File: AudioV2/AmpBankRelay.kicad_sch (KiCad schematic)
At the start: 20 parts, among them K301 AZ850P2-5, K302 AZ850P2-5, K303 AZ850P2-5, K304 AZ850P2-5, U321 TBD62083APG

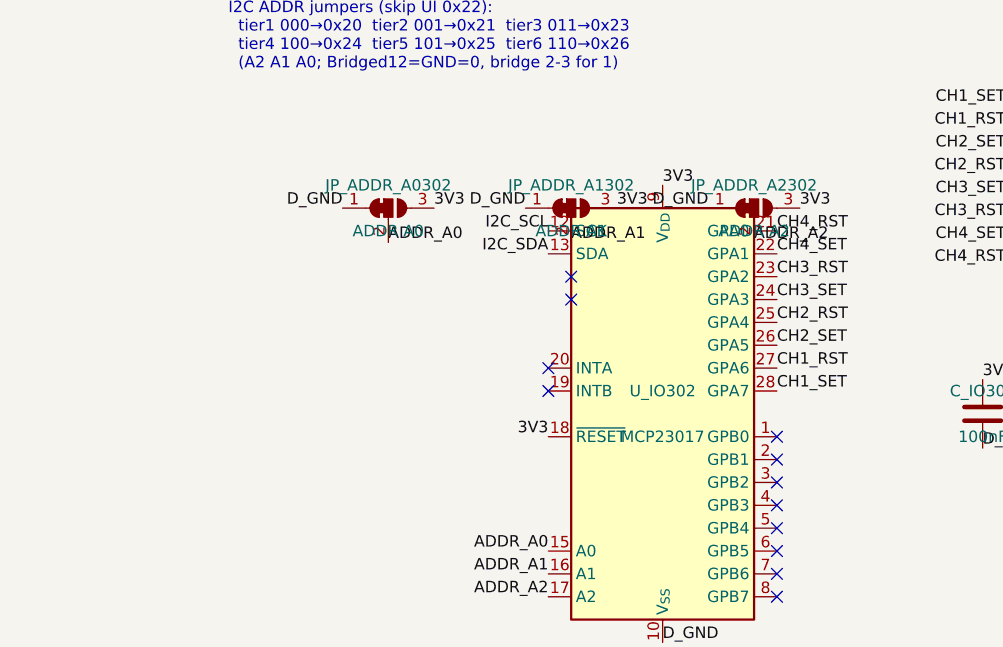
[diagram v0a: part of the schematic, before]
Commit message: AudioV2: ADDR ジャンパ参照を S_/R_ に揃え、早見表シルクを見やすく
Switch/Relay のジャンパを S_ADDR_* / R_ADDR_* に改名し、PCB シルクの番地表記を A2/A1/A0 形式に更新。

Co-authored-by: Cursor <cursoragent@cursor.com>
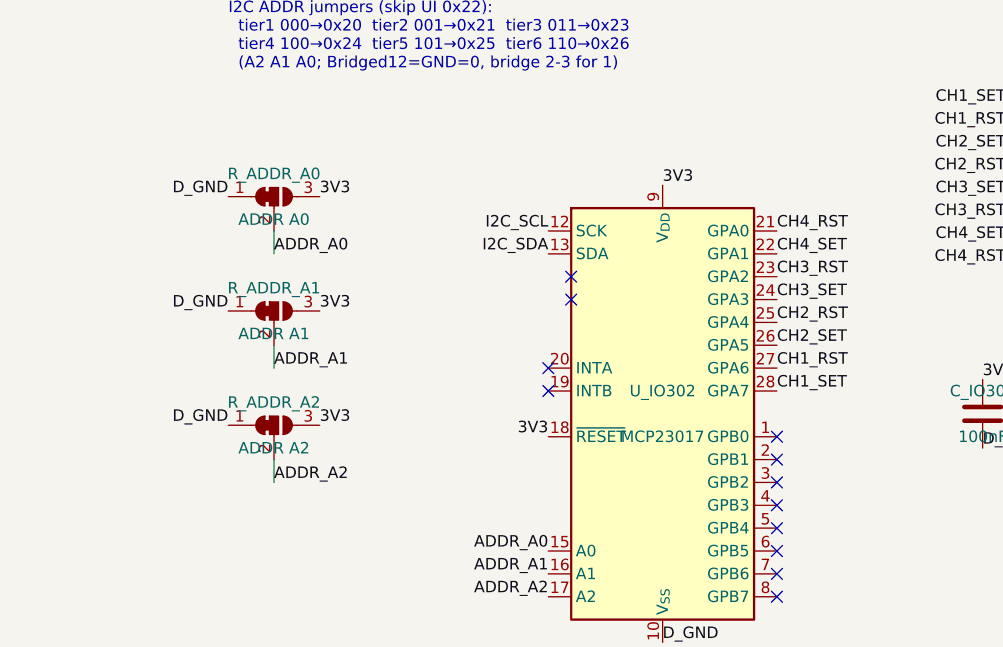
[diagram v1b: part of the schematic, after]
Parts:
- renumbered JP_ADDR_A0302 to R_ADDR_A0, JP_ADDR_A1302 to R_ADDR_A1, JP_ADDR_A2302 to R_ADDR_A2
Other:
- moved on the sheet: R_ADDR_A0, R_ADDR_A1, R_ADDR_A2
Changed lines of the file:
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@@
 		(at 284.48 281.94)
+	)
+	(wire
+		(pts
+			(xy 157.48 220.98) (xy 157.48 218.44)
+		)
+		(stroke
+			(width 0)
+			(type default)
+		)
+	)
+	(wire
+		(pts
+			(xy 157.48 208.28) (xy 157.48 205.74)
+		)
+		(stroke
+			(width 0)
+			(type default)
+		)
+	)
+	(wire
+		(pts
+			(xy 157.48 195.58) (xy 157.48 193.04)
+		)
+		(stroke
+			(width 0)
+			(type default)
+		)
 	)
 	(label "CH1_OUT_R"
@@
 	)
 	(label "D_GND"
-		(at 205.74 190.5 180)
+		(at 152.4 214.63 180)
 		(effects
 			(font
@@
 	)
 	(label "ADDR_A2"
-		(at 210.82 194.31 0)
+		(at 157.48 220.98 0)
 		(effects
 			(font
@@
 	)
 	(label "3V3"
-		(at 195.58 190.5 0)
+		(at 162.56 201.93 0)
 		(effects
 			(font
@@
 	)
 	(label "D_GND"
-		(at 165.1 190.5 180)
+		(at 152.4 189.23 180)
 		(effects
 			(font
@@
 	)
 	(label "3V3"
-		(at 215.9 190.5 0)
+		(at 162.56 214.63 0)
 		(effects
 			(font
@@
 	)
 	(label "3V3"
-		(at 175.26 190.5 0)
+		(at 162.56 189.23 0)
 		(effects
 			(font
@@
 	)
 	(label "D_GND"
-		(at 185.42 190.5 180)
+		(at 152.4 201.93 180)
 		(effects
 			(font
@@
 	)
 	(label "ADDR_A1"
-		(at 190.5 194.31 0)
+		(at 157.48 208.28 0)
 		(effects
 			(font
@@
 	)
 	(label "ADDR_A0"
-		(at 170.18 194.31 0)
+		(at 157.48 195.58 0)
 		(effects
 			(font
@@
 	(symbol
 		(lib_id "Jumper:SolderJumper_3_Bridged12")
-		(at 170.18 190.5 0)
+		(at 157.48 189.23 0)
 		(unit 1)
 		(body_style 1)
@@
 		(dnp no)
 		(fields_autoplaced yes)
-		(property "Reference" "JP_ADDR_A0302"
-			(at 170.18 187.96 0)
+		(property "Reference" "R_ADDR_A0"
+			(at 157.48 186.69 0)
 			(show_name no)
 			(do_not_autoplace no)
@@
 		)
 		(property "Value" "ADDR A0"
-			(at 170.18 193.04 0)
+			(at 157.48 191.77 0)
 			(show_name no)
 			(do_not_autoplace no)
@@
 		)
 		(property "Footprint" "Jumper:SolderJumper-3_P1.3mm_Bridged12_Pad1.0x1.5mm_NumberLabels"
-			(at 0 0 0)
+			(at -12.7 -1.27 0)
 			(hide yes)
 			(show_name no)
@@
 		)
 		(property "Datasheet" ""
-			(at 0 0 0)
+			(at -12.7 -1.27 0)
 			(hide yes)
 			(show_name no)
@@
 		)
 		(property "Description" ""
-			(at 0 0 0)
+			(at -12.7 -1.27 0)
 			(hide yes)
 			(show_name no)
@@
 			(project "AudioV2Case"
 				(path "/a1000001-0001-4001-8001-000000000001/a1000013-0013-4013-8013-000000000013"
-					(reference "JP_ADDR_A0302")
+					(reference "R_ADDR_A0")
 					(unit 1)
 				)
@@
 	(symbol
 		(lib_id "Jumper:SolderJumper_3_Bridged12")
-		(at 190.5 190.5 0)
+		(at 157.48 201.93 0)
 		(unit 1)
 		(body_style 1)
@@
 		(dnp no)
 		(fields_autoplaced yes)
-		(property "Reference" "JP_ADDR_A1302"
-			(at 190.5 187.96 0)
+		(property "Reference" "R_ADDR_A1"
+			(at 157.48 199.39 0)
 			(show_name no)
 			(do_not_autoplace no)
@@
 		)
 		(property "Value" "ADDR A1"
-			(at 190.5 193.04 0)
+			(at 157.48 204.47 0)
 			(show_name no)
 			(do_not_autoplace no)
@@
 		)
 		(property "Footprint" "Jumper:SolderJumper-3_P1.3mm_Bridged12_Pad1.0x1.5mm_NumberLabels"
-			(at 0 0 0)
+			(at -33.02 11.43 0)
 			(hide yes)
 			(show_name no)
@@
 		)
 		(property "Datasheet" ""
-			(at 0 0 0)
+			(at -33.02 11.43 0)
 			(hide yes)
 			(show_name no)
@@
 		)
 		(property "Description" ""
-			(at 0 0 0)
+			(at -33.02 11.43 0)
 			(hide yes)
 			(show_name no)
@@
 			(project "AudioV2Case"
 				(path "/a1000001-0001-4001-8001-000000000001/a1000013-0013-4013-8013-000000000013"
-					(reference "JP_ADDR_A1302")
+					(reference "R_ADDR_A1")
 					(unit 1)
 				)
@@
 	(symbol
 		(lib_id "Jumper:SolderJumper_3_Bridged12")
-		(at 210.82 190.5 0)
+		(at 157.48 214.63 0)
 		(unit 1)
 		(body_style 1)
@@
 		(dnp no)
 		(fields_autoplaced yes)
-		(property "Reference" "JP_ADDR_A2302"
-			(at 210.82 187.96 0)
+		(property "Reference" "R_ADDR_A2"
+			(at 157.48 212.09 0)
 			(show_name no)
 			(do_not_autoplace no)
@@
 		)
 		(property "Value" "ADDR A2"
-			(at 210.82 193.04 0)
+			(at 157.48 217.17 0)
 			(show_name no)
 			(do_not_autoplace no)
@@
 		)
 		(property "Footprint" "Jumper:SolderJumper-3_P1.3mm_Bridged12_Pad1.0x1.5mm_NumberLabels"
-			(at 0 0 0)
+			(at -53.34 24.13 0)
 			(hide yes)
 			(show_name no)
@@
 		)
 		(property "Datasheet" ""
-			(at 0 0 0)
+			(at -53.34 24.13 0)
 			(hide yes)
 			(show_name no)
@@
 		)
 		(property "Description" ""
-			(at 0 0 0)
+			(at -53.34 24.13 0)
 			(hide yes)
 			(show_name no)
@@
 			(project "AudioV2Case"
 				(path "/a1000001-0001-4001-8001-000000000001/a1000013-0013-4013-8013-000000000013"
-					(reference "JP_ADDR_A2302")
+					(reference "R_ADDR_A2")
 					(unit 1)
 				)

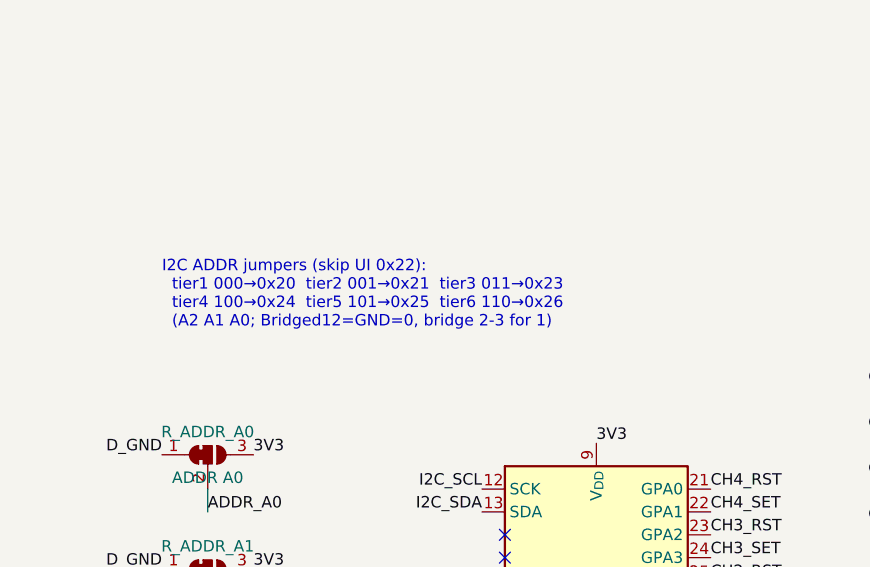
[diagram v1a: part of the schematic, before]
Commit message: AudioV2: ADDR 参照・注記を build_daughter に書き戻す
Relay ジャンパを R_ADDR_A* にし、番地早見の文言を sch/PCB と揃えた。再生成はしていない。

Co-authored-by: Cursor <cursoragent@cursor.com>
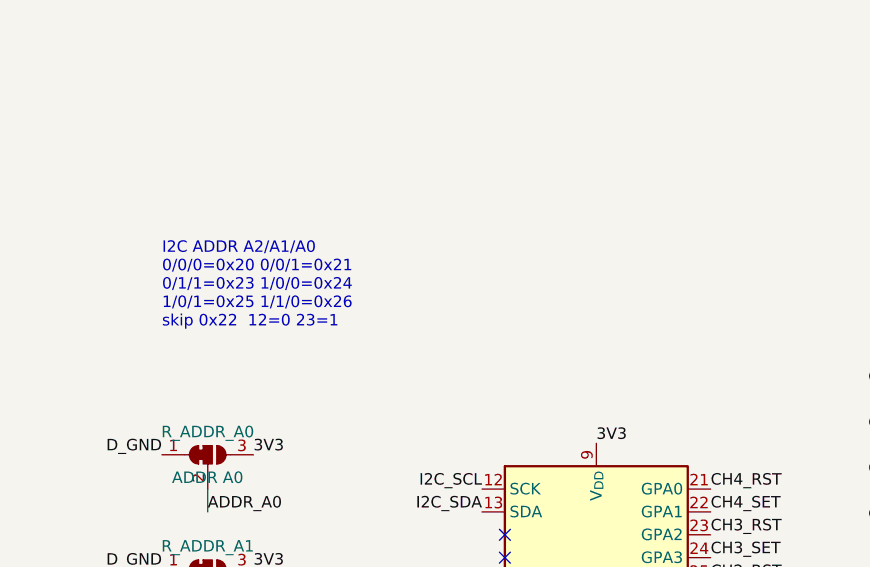
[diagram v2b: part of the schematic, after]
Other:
- note added: "I2C ADDR A2/A1/A0 0/0/0=0x20 0/0/1=0x21 0/1/1=0x23 1/0/0=0x24 1/0/1=0x25 1/1/0=0x26 skip 0x22 12=0 23=1"
- note removed: "I2C ADDR jumpers (skip UI 0x22): tier1 000→0x20 tier2 001→0x21 tier3 011→0x23 tier4 100→0x24 tier5 101→0x25 tier6 110→0x26 (A2 A1 A0; Bridged12=GND=0, bridge 2-3 for 1)"
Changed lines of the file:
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@@
 	(generator_version "10.0")
 	(paper "A2")
-	(text "I2C ADDR jumpers (skip UI 0x22):\n  tier1 000→0x20  tier2 001→0x21  tier3 011→0x23\n  tier4 100→0x24  tier5 101→0x25  tier6 110→0x26\n  (A2 A1 A0; Bridged12=GND=0, bridge 2-3 for 1)"
+	(text "I2C ADDR A2/A1/A0
+0/0/0=0x20 0/0/1=0x21
+0/1/1=0x23 1/0/0=0x24
+1/0/1=0x25 1/1/0=0x26
+skip 0x22  12=0 23=1"
 		(exclude_from_sim no)
 		(at 152.4 175.26 0)

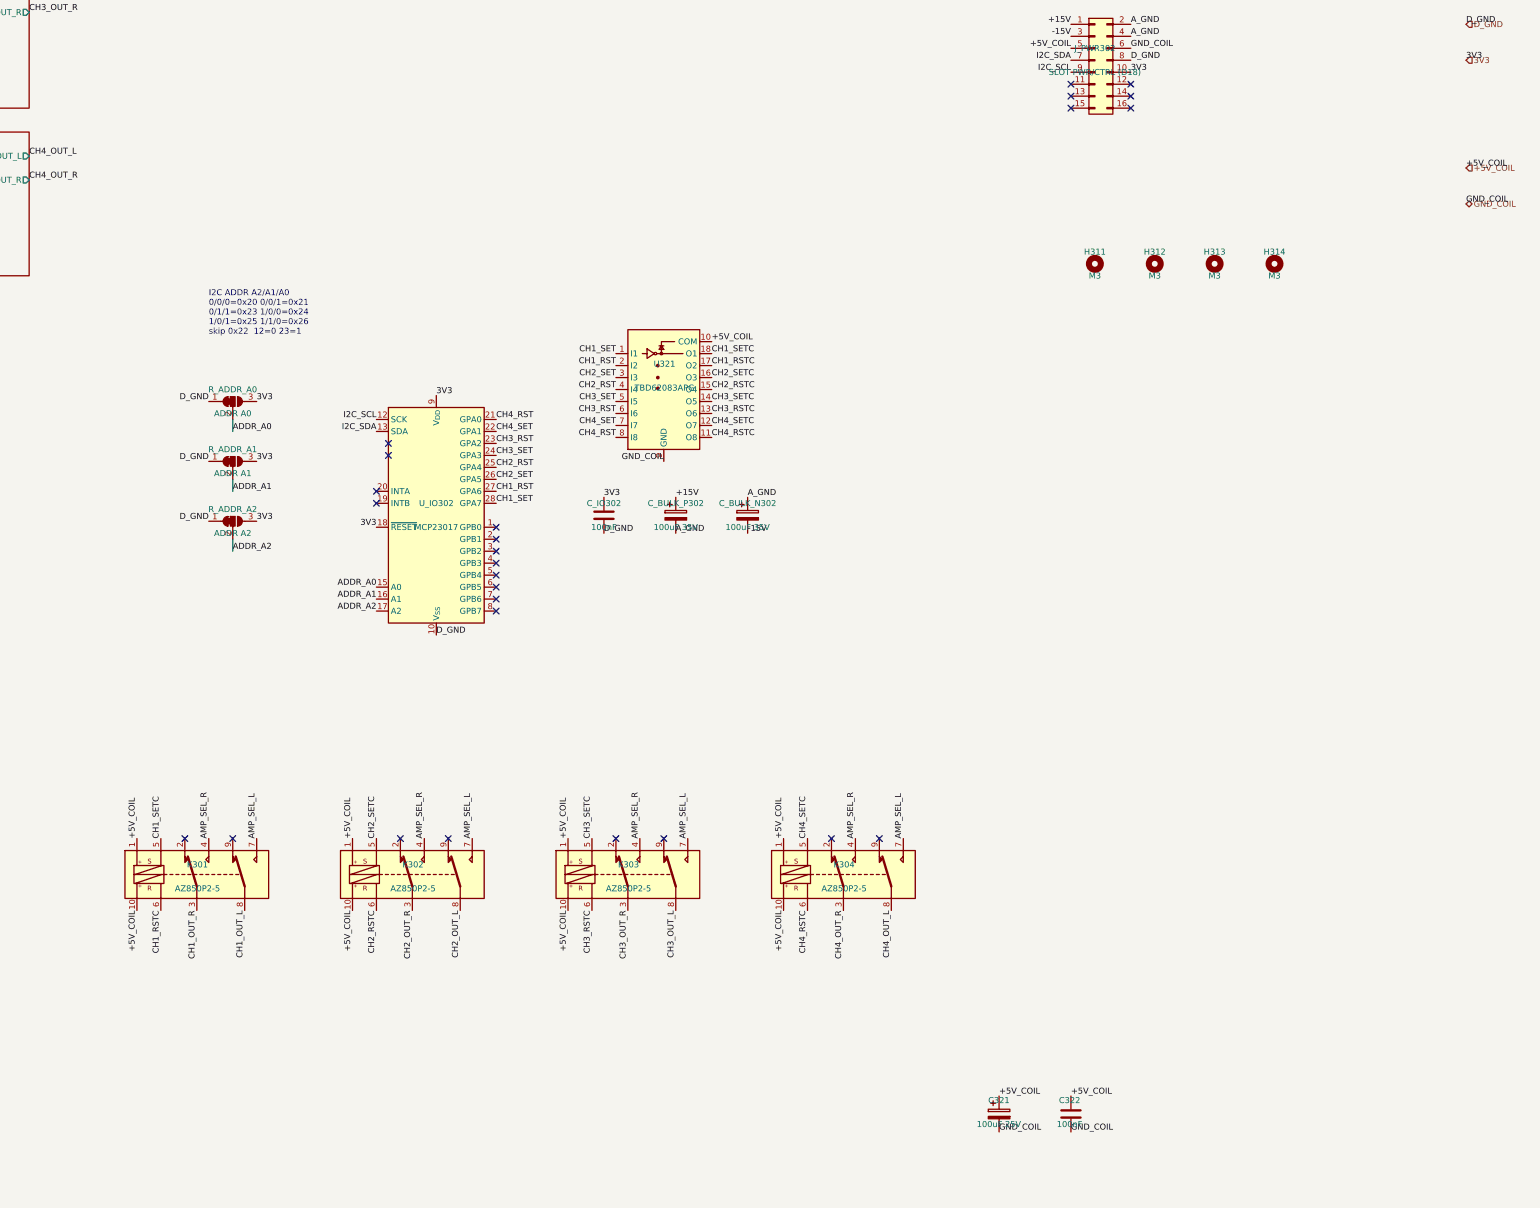
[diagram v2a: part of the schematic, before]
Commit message: AudioV2: Switch の MCP／S_ADDR も build_daughter で生成する
再生成で Switch の ADDR／MCP が消えないように両版をスクリプトに載せ、娘を再生成した。

Co-authored-by: Cursor <cursoragent@cursor.com>
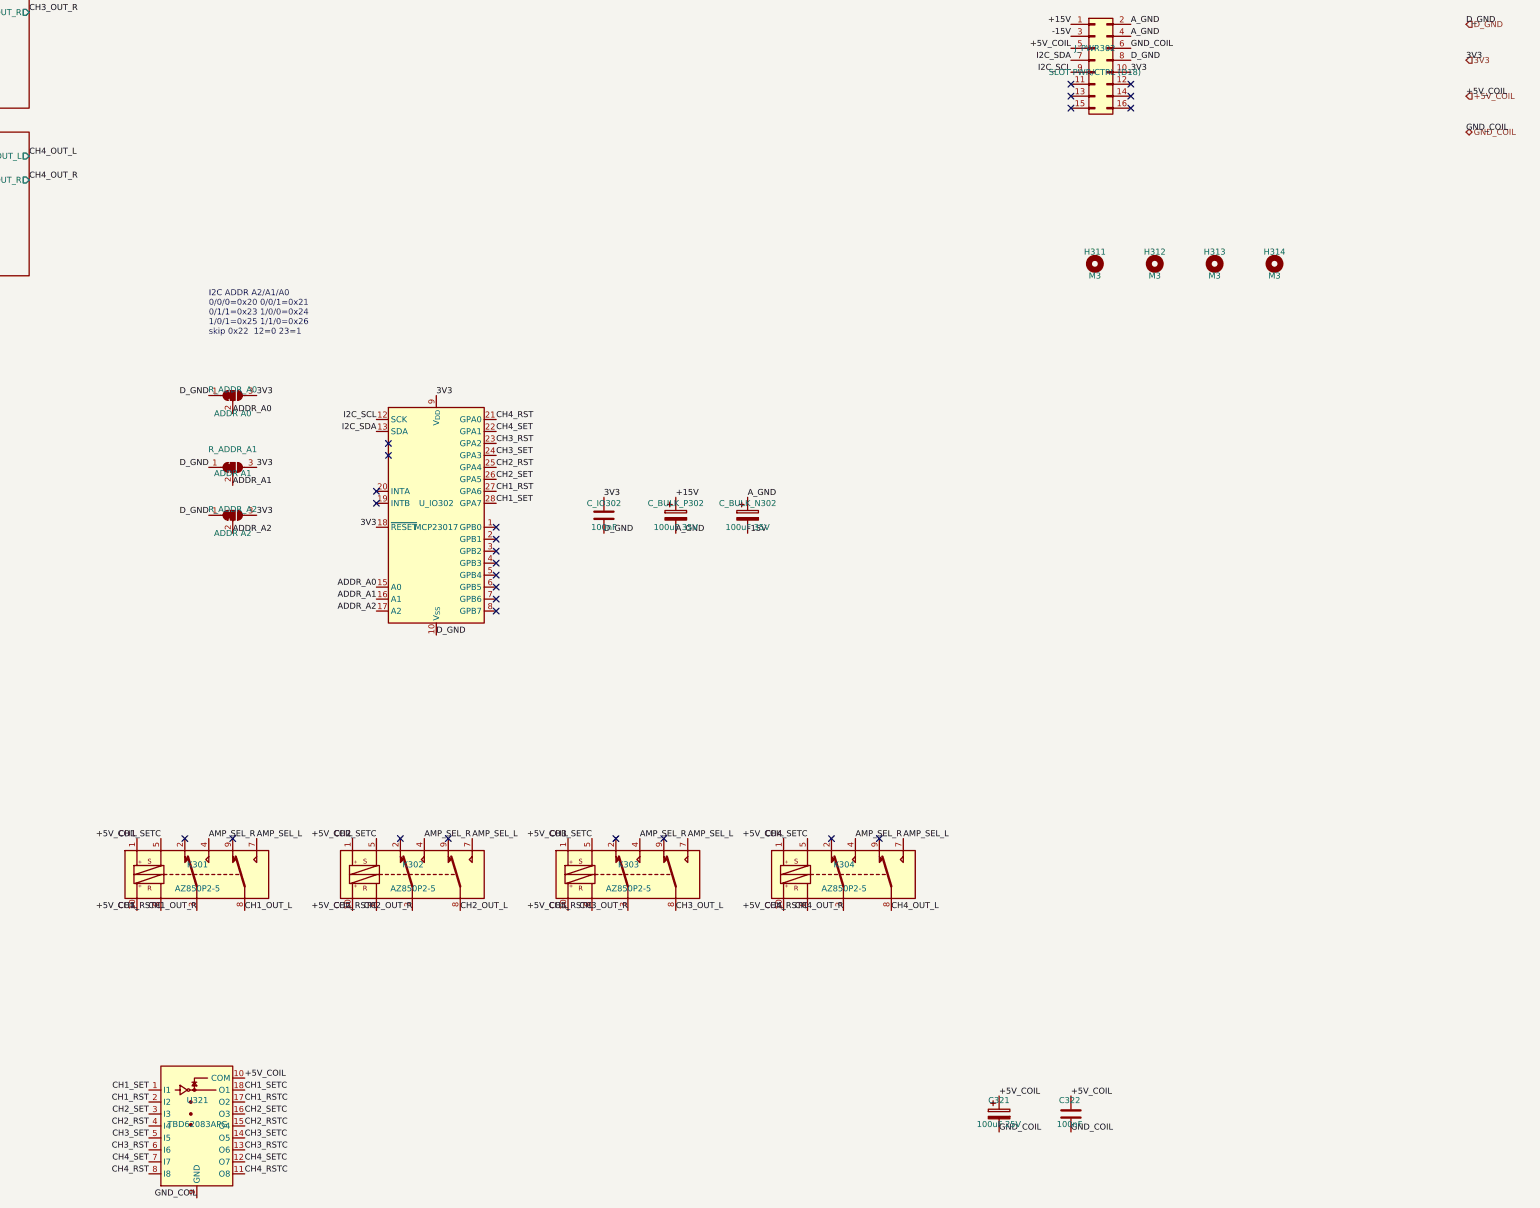
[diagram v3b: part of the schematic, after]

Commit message: AudioV2: 親スロットを ANA/PWR 各1組（101）に減らす
当面は Switch 娘1枚前提。102/103 を回路図と PCB から外した。

Co-authored-by: Cursor <cursoragent@cursor.com>
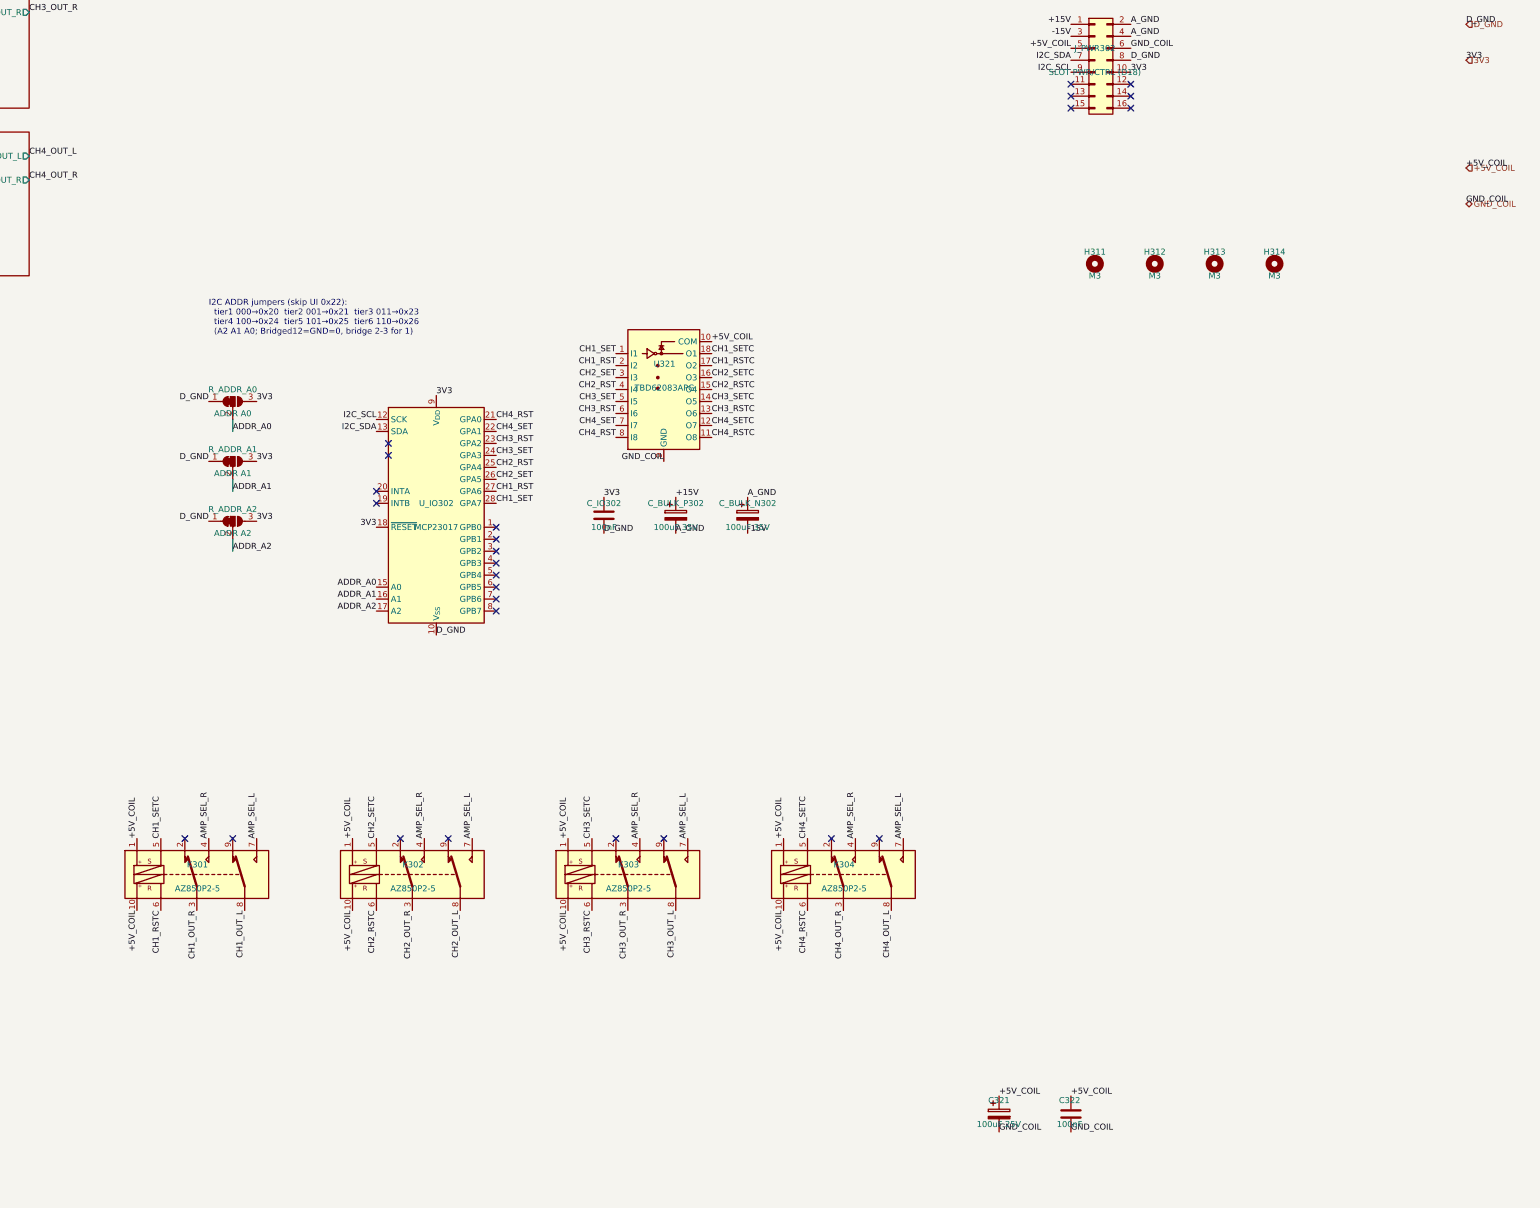
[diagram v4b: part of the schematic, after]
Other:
- note added: "I2C ADDR jumpers (skip UI 0x22): tier1 000→0x20 tier2 001→0x21 tier3 011→0x23 tier4 100→0x24 tier5 101→0x25 tier6 110→0x26 (A2 A1 A0; Bridged12=GND=0, bridge 2-3 for 1)"
- note removed: "I2C ADDR A2/A1/A0 0/0/0=0x20 0/0/1=0x21 0/1/1=0x23 1/0/0=0x24 1/0/1=0x25 1/1/0=0x26 skip 0x22 12=0 23=1"
